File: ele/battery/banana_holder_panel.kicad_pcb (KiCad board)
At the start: 2 copper layers, 100 x 100 mm, 72 parts, among them J30 mech

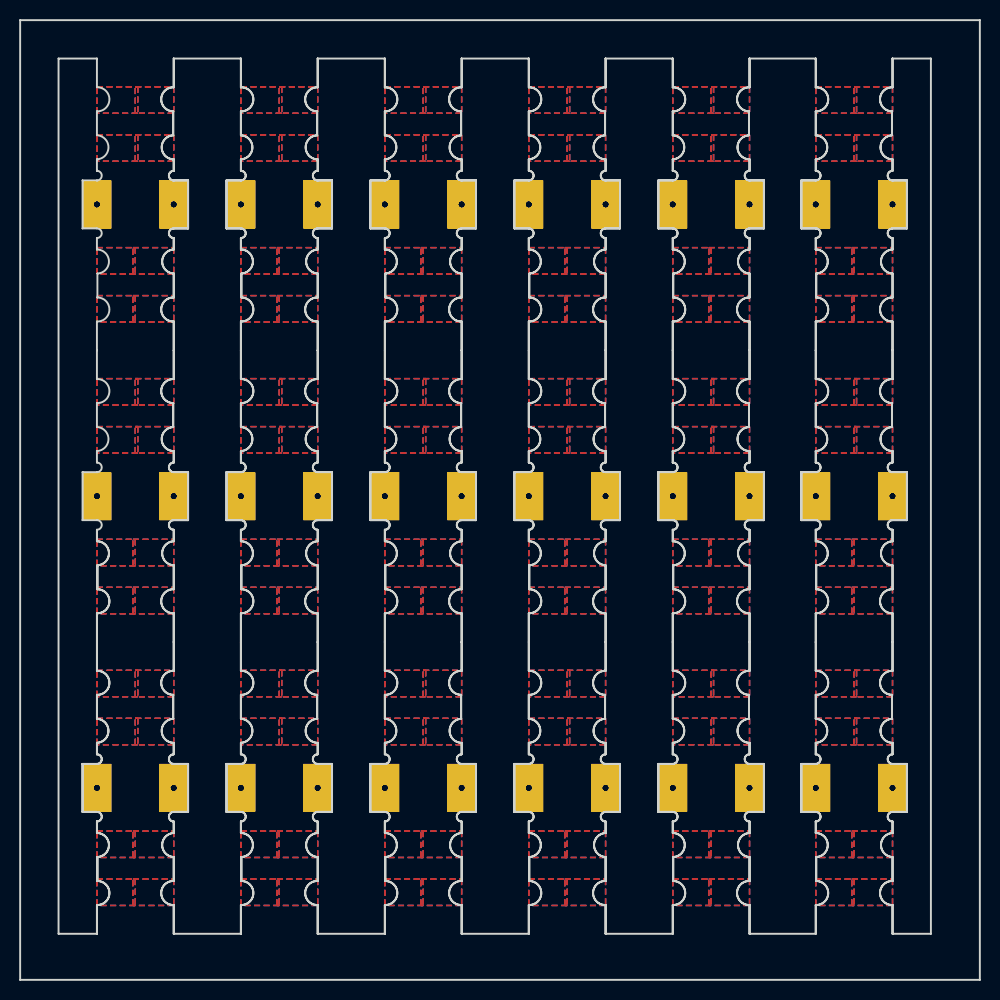
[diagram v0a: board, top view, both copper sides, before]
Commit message: ele: Update battery panels
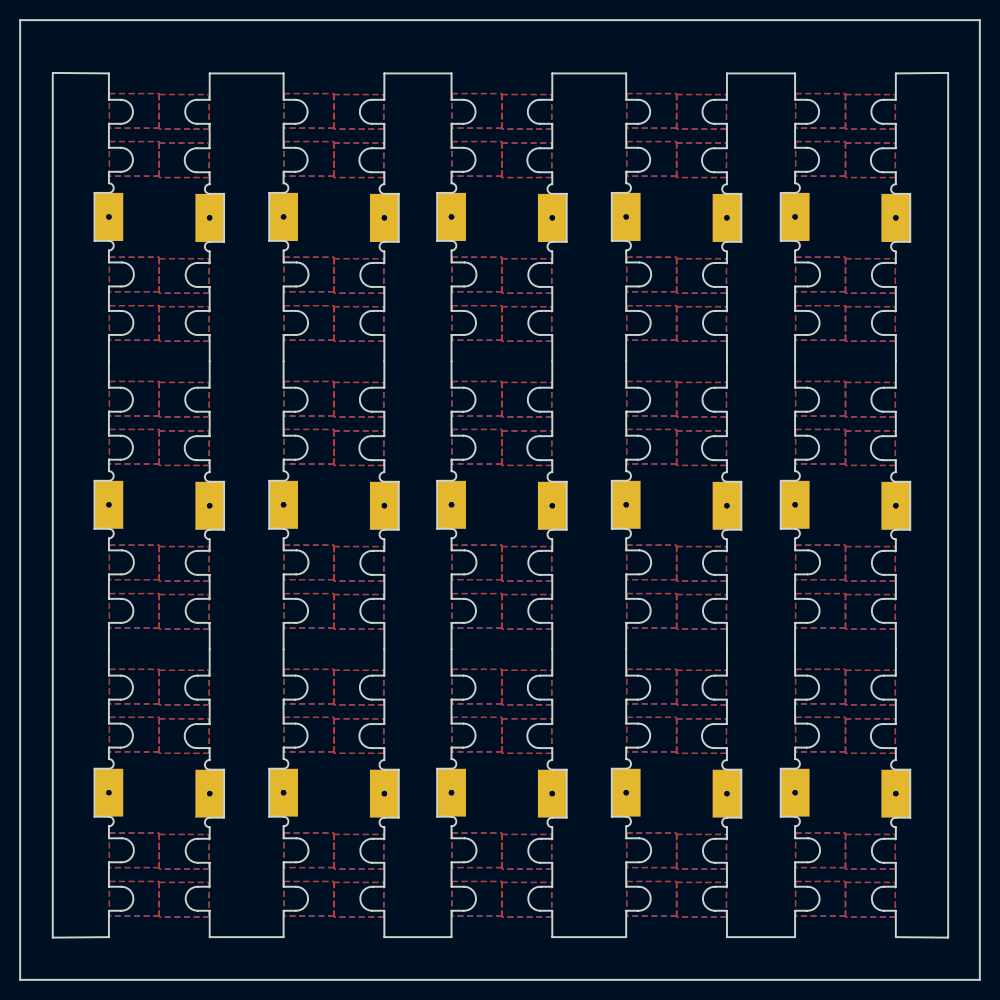
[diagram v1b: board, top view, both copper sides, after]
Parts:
- removed the J30 at (156.9, 154.6) (x2)
- removed the J30 at (148.9, 154.6) (x2)
- removed the J30 at (156.9, 124.2) (x2)
- removed the J30 at (134.0, 124.2) (x2)
- removed the J30 at (142.0, 93.8) (x2)
- removed the J30 at (134.0, 154.6) (x2)
- removed the J30 at (134.0, 93.8) (x2)
- removed the J30 at (142.0, 124.2) (x2)
- removed the J30 at (148.9, 93.8) (x2)
- removed the J30 at (142.0, 154.6) (x2)
- removed the J30 at (119.0, 124.2) (x2)
- removed the J30 at (119.0, 93.8) (x2)
- removed the J30 at (127.0, 124.2) (x2)
- removed the J30 at (119.0, 154.6) (x2)
- removed the J30 at (127.0, 93.8) (x2)
- removed the J30 at (127.0, 154.6) (x2)
- removed the J30 at (112.0, 154.6) (x2)
- removed the J30 at (104.0, 93.8) (x2)
- removed the J30 at (148.9, 124.2) (x2)
- removed the J30 at (104.0, 124.2) (x2)
- removed the J30 at (112.0, 93.8) (x2)
- removed the J30 at (112.0, 124.2) (x2)
- removed the J30 at (104.0, 154.6) (x2)
- removed the J30 at (97.0, 124.2) (x2)
- removed the J30 at (89.0, 124.2) (x2)
- removed the J30 at (97.0, 154.6) (x2)
- removed the J30 at (89.0, 93.8) (x2)
- removed the J30 at (97.0, 93.8) (x2)
- removed the J30 at (89.0, 154.6) (x2)
- removed the J30 at (156.9, 93.8) (x2)
- removed the J30 at (82.0, 124.2) (x2)
- removed the J30 at (74.0, 124.2) (x2)
- removed the J30 at (74.0, 154.6) (x2)
- removed the J30 at (82.0, 154.6) (x2)
- removed the J30 at (82.0, 93.8) (x2)
- removed the J30 at (74.0, 93.8) (x2)
- added J30: mech, BATTERY:pad_3x5, F.Cu at (157.2, 95.2)
- added J30: mech, BATTERY:pad_3x5, F.Cu at (129.2, 155.1)
- added J30: mech, BATTERY:pad_3x5, F.Cu at (139.7, 95.2)
- added J30: mech, BATTERY:pad_3x5, F.Cu at (129.2, 125.0)
- added J30: mech, BATTERY:pad_3x5, F.Cu at (121.5, 95.2)
- added J30: mech, BATTERY:pad_3x5, F.Cu at (111.0, 125.0)
- added J30: mech, BATTERY:pad_3x5, F.Cu at (111.0, 155.1)
- added J30: mech, BATTERY:pad_3x5, F.Cu at (121.5, 155.2)
- added J30: mech, BATTERY:pad_3x5, F.Cu at (121.5, 125.2)
- added J30: mech, BATTERY:pad_3x5, F.Cu at (111.0, 95.0)
- added J30: mech, BATTERY:pad_3x5, F.Cu at (93.5, 95.0)
- added J30: mech, BATTERY:pad_3x5, F.Cu at (146.8, 95.0)
- added J30: mech, BATTERY:pad_3x5, F.Cu at (104.0, 125.2)
- added J30: mech, BATTERY:pad_3x5, F.Cu at (104.0, 155.2)
- added J30: mech, BATTERY:pad_3x5, F.Cu at (93.5, 155.1)
- added J30: mech, BATTERY:pad_3x5, F.Cu at (93.5, 125.0)
- added J30: mech, BATTERY:pad_3x5, F.Cu at (104.0, 95.2)
- added J30: mech, BATTERY:pad_3x5, F.Cu at (85.8, 155.2)
- added J30: mech, BATTERY:pad_3x5, F.Cu at (75.2, 155.1)
- added J30: mech, BATTERY:pad_3x5, F.Cu at (75.2, 125.0)
- added J30: mech, BATTERY:pad_3x5, F.Cu at (85.8, 125.2)
- added J30: mech, BATTERY:pad_3x5, F.Cu at (75.2, 95.0)
- added J30: mech, BATTERY:pad_3x5, F.Cu at (146.8, 125.0)
- added J30: mech, BATTERY:pad_3x5, F.Cu at (85.8, 95.2)
- added J30: mech, BATTERY:pad_3x5, F.Cu at (157.2, 125.2)
- added J30: mech, BATTERY:pad_3x5, F.Cu at (157.2, 155.2)
- added J30: mech, BATTERY:pad_3x5, F.Cu at (146.8, 155.1)
- added J30: mech, BATTERY:pad_3x5, F.Cu at (139.7, 125.2)
- added J30: mech, BATTERY:pad_3x5, F.Cu at (139.7, 155.2)
- added J30: mech, BATTERY:pad_3x5, F.Cu at (129.2, 95.0)
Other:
- outline, holes or cut-outs redrawn
